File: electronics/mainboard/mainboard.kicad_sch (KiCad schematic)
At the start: 1 part, among them U1 1022

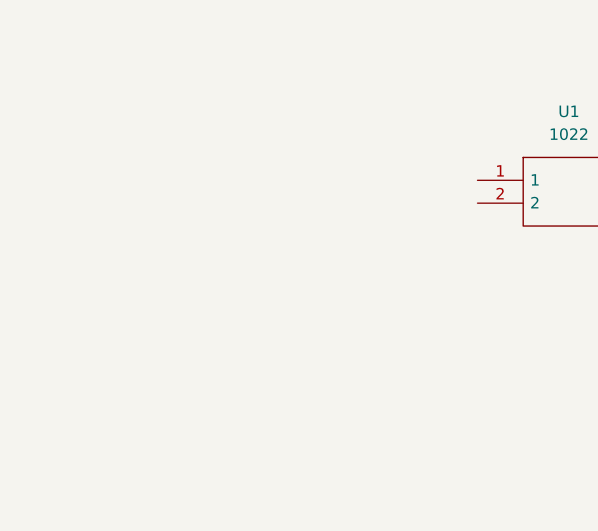
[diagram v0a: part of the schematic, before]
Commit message: add arduino nano to pcb
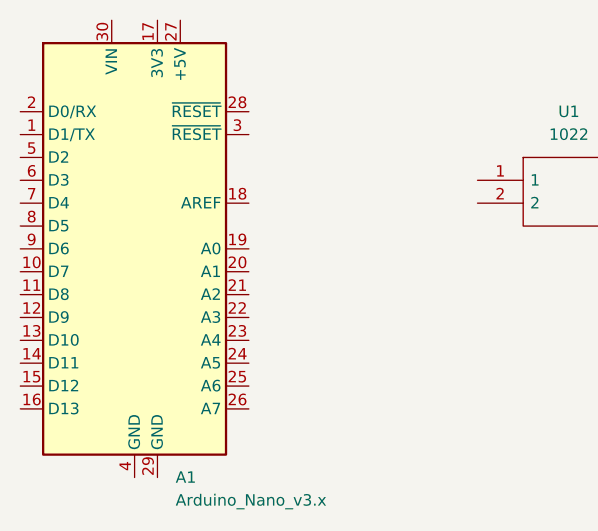
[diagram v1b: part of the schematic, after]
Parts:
- added A1: Arduino_Nano_v3.x, Module:Arduino_Nano_WithMountingHoles, symbol MCU_Module:Arduino_Nano_v3.x
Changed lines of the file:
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@@
     (pin "4")
+  )
+  (symbol (lib_id "MCU_Module:Arduino_Nano_v3.x") (at 106.68 95.25 0) (unit 1)
+    (in_bom yes) (on_board yes) (fields_autoplaced)
+    (property "Reference" "A1" (id 0) (at 111.2394 120.65 0)
+      (effects (font (size 1.27 1.27)) (justify left))
+    )
+    (property "Value" "Arduino_Nano_v3.x" (id 1) (at 111.2394 123.19 0)
+      (effects (font (size 1.27 1.27)) (justify left))
+    )
+    (property "Footprint" "Module:Arduino_Nano_WithMountingHoles" (id 2) (at 106.68 95.25 0)
+      (effects (font (size 1.27 1.27) italic) hide)
+    )
+    (property "Datasheet" "http://www.mouser.com/pdfdocs/Gravitech_Arduino_Nano3_0.pdf" (id 3) (at 106.68 95.25 0)
+      (effects (font (size 1.27 1.27)) hide)
+    )
+    (pin "1")
+    (pin "10")
+    (pin "11")
+    (pin "12")
+    (pin "13")
+    (pin "14")
+    (pin "15")
+    (pin "16")
+    (pin "17")
+    (pin "18")
+    (pin "19")
+    (pin "2")
+    (pin "20")
+    (pin "21")
+    (pin "22")
+    (pin "23")
+    (pin "24")
+    (pin "25")
+    (pin "26")
+    (pin "27")
+    (pin "28")
+    (pin "29")
+    (pin "3")
+    (pin "30")
+    (pin "4")
+    (pin "5")
+    (pin "6")
+    (pin "7")
+    (pin "8")
+    (pin "9")
   )
   (sheet_instances
@@
   )
   (symbol_instances
+    (path "/8fac398c-22c9-4741-a001-aab7ea92da04"
+      (reference "A1") (unit 1) (value "Arduino_Nano_v3.x") (footprint "Module:Arduino_Nano_WithMountingHoles")
+    )
     (path "/59142adb-6887-41fc-851e-9a7f51511d60"
       (reference "U1") (unit 1) (value "1022") (footprint "SamacSys:1022")

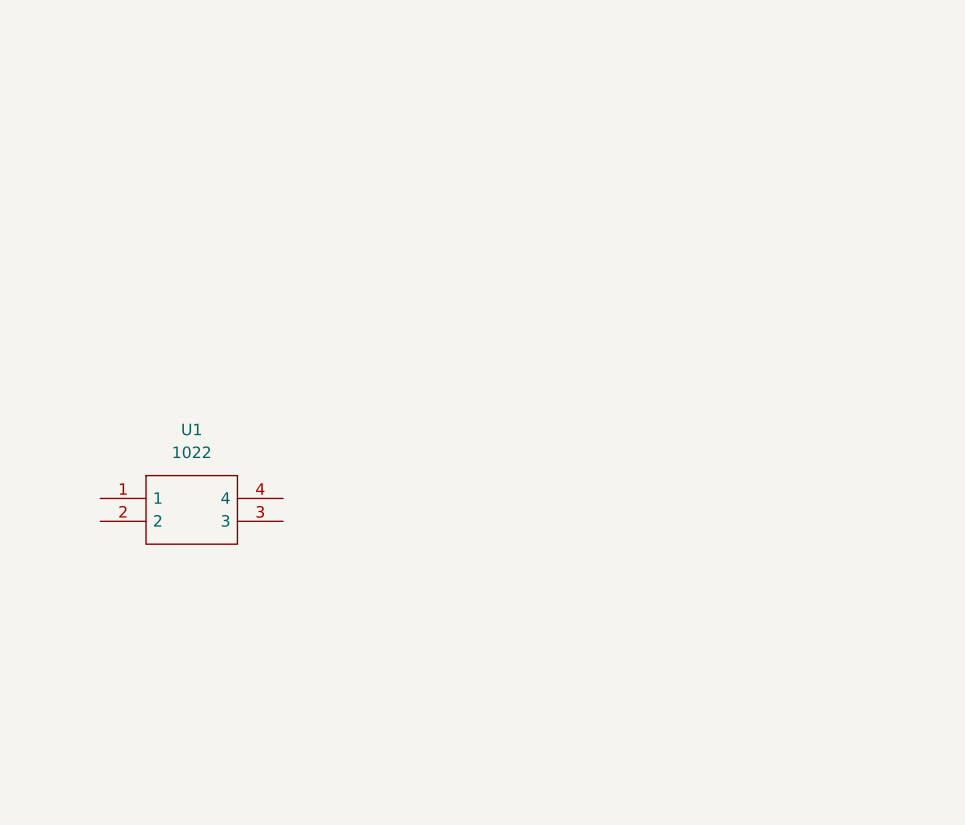
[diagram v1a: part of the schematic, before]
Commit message: add buttons and ir-led
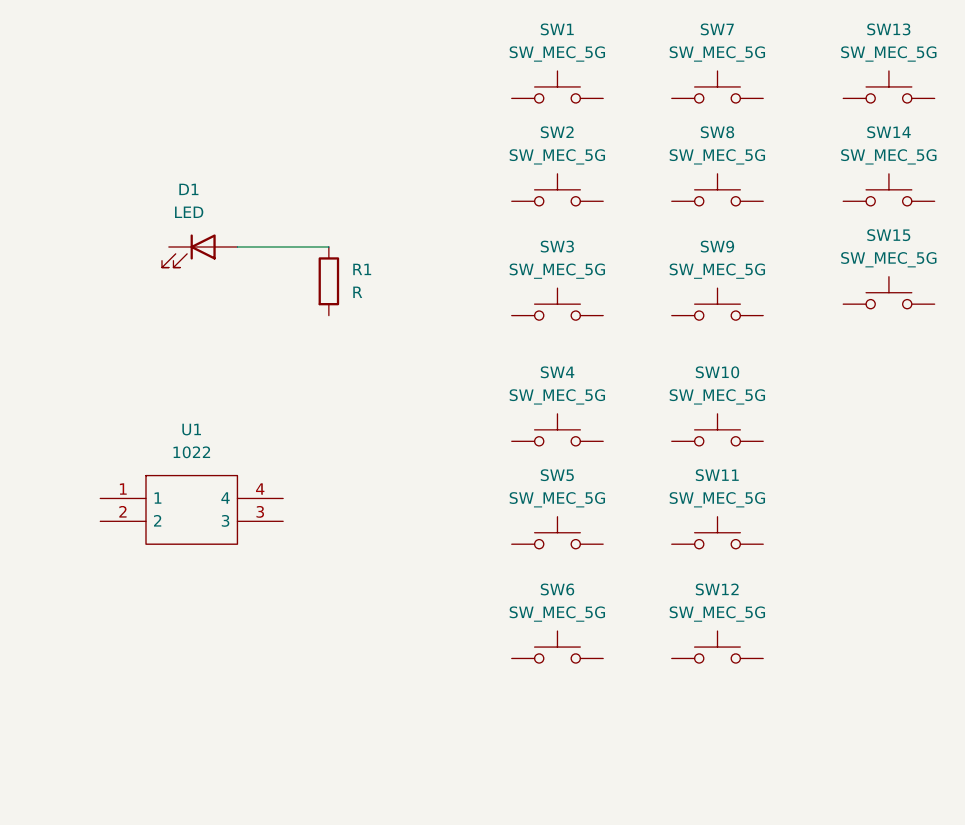
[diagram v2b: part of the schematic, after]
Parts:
- added D1: LED, LED_THT:LED_D5.0mm_Horizontal_O1.27mm_Z3.0mm, symbol Device:LED
- added R1: R, Resistor_SMD:R_0805_2012Metric, symbol Device:R
- added SW1, SW10, SW11, SW12, SW13, SW14, SW15, SW2, SW3, SW4, SW5, SW6, SW7, SW8, SW9: SW_MEC_5G, Button_Switch_THT:SW_PUSH_6mm, symbol Switch:SW_MEC_5G
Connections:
- new net: SW11.1 (A), SW11.2 (A)
- new net: SW11.3 (B), SW11.4 (B)
- new net: D1.2 (A), R1.1
- new net: SW5.1 (A), SW5.2 (A)
- new net: SW5.3 (B), SW5.4 (B)
- new net: SW2.1 (A), SW2.2 (A)
- new net: SW2.3 (B), SW2.4 (B)
- new net: SW8.1 (A), SW8.2 (A)
- new net: SW8.3 (B), SW8.4 (B)
- new net: SW3.1 (A), SW3.2 (A)
- new net: SW3.3 (B), SW3.4 (B)
- new net: SW7.1 (A), SW7.2 (A)
- new net: SW7.3 (B), SW7.4 (B)
- new net: SW12.1 (A), SW12.2 (A)
- new net: SW12.3 (B), SW12.4 (B)
- new net: SW9.1 (A), SW9.2 (A)
- new net: SW9.3 (B), SW9.4 (B)
- new net: SW10.1 (A), SW10.2 (A)
- new net: SW10.3 (B), SW10.4 (B)
- new net: SW13.1 (A), SW13.2 (A)
- new net: SW13.3 (B), SW13.4 (B)
- new net: SW14.1 (A), SW14.2 (A)
- new net: SW14.3 (B), SW14.4 (B)
- new net: SW15.1 (A), SW15.2 (A)
- new net: SW15.3 (B), SW15.4 (B)
- new net: SW4.1 (A), SW4.2 (A)
- new net: SW4.3 (B), SW4.4 (B)
- new net: SW1.1 (A), SW1.2 (A)
- new net: SW1.3 (B), SW1.4 (B)
- new net: SW6.1 (A), SW6.2 (A)
- new net: SW6.3 (B), SW6.4 (B)

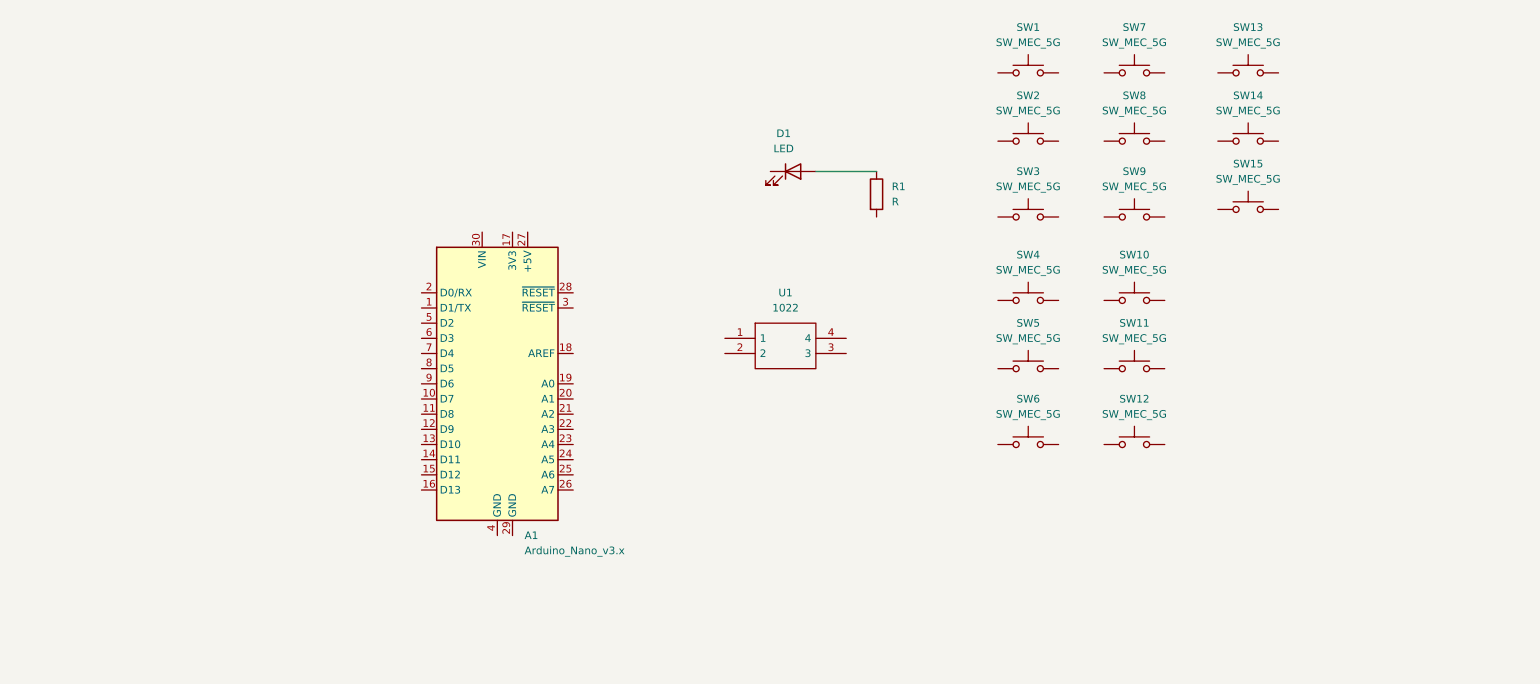
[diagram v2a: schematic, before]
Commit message: add schematic connections
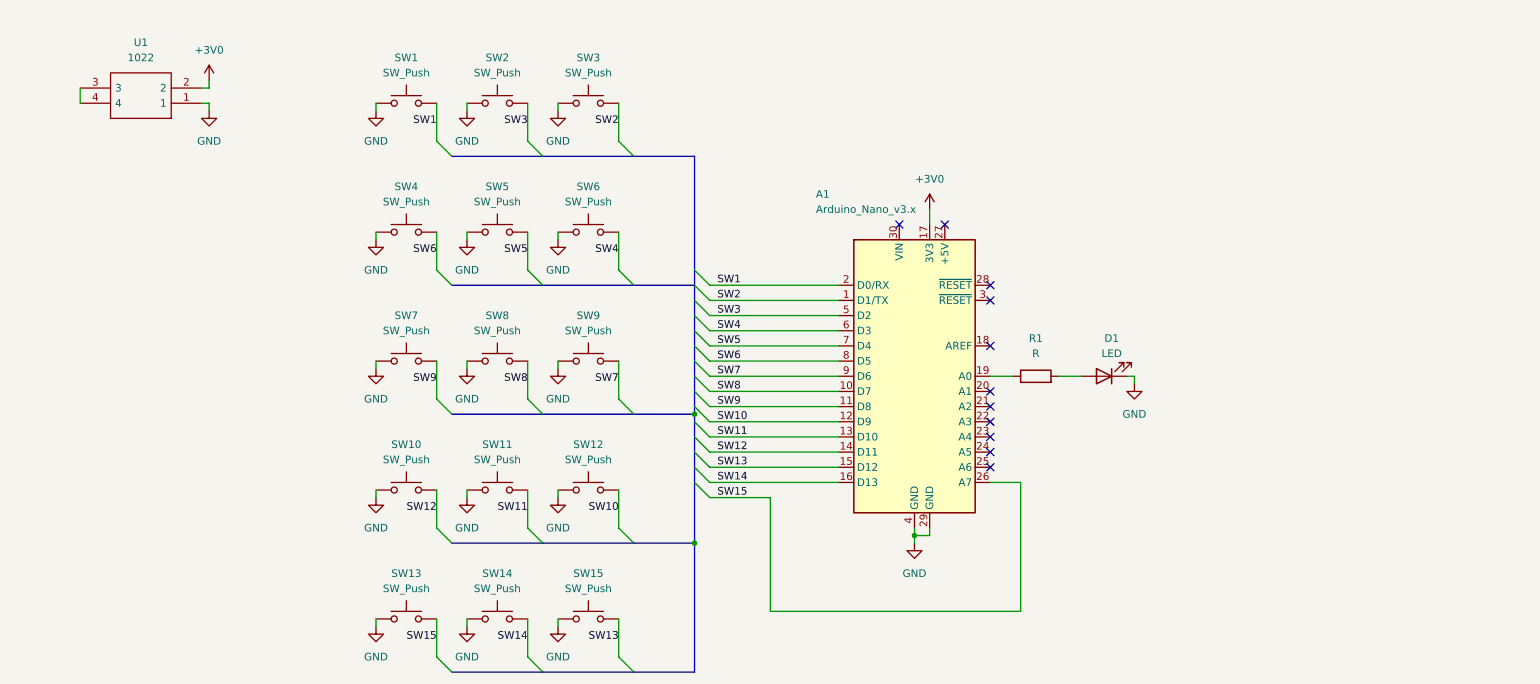
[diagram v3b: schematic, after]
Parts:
- removed SW1, SW10, SW11, SW12, SW13, SW14, SW15, SW2, SW3, SW4, SW5, SW6, SW7, SW8, SW9: SW_MEC_5G, Button_Switch_THT:SW_PUSH_6mm, symbol Switch:SW_MEC_5G
- added SW1, SW10, SW11, SW12, SW13, SW14, SW15, SW2, SW3, SW4, SW5, SW6, SW7, SW8, SW9: SW_Push, Button_Switch_THT:SW_PUSH_6mm, symbol Switch:SW_Push
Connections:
- net at R1.1: now also A1.19 (A0); no longer D1.2 (A)
- net at R1.2: now also D1.2 (A)
- net GND: now reaches U1.1
- net GND: now also A1.29 (GND), A1.4 (GND), D1.1 (K), SW1.1, SW10.1, SW11.1, SW12.1, SW13.1, SW14.1, SW15.1, SW2.1, SW3.1, SW4.1, SW5.1, SW6.1, SW7.1, SW8.1, SW9.1
- net +3V0: now reaches U1.2
- net +3V0: now also A1.17 (3V3)
- net at U1.3: now also U1.4
- net SW2: now reaches A1.1 (D1/TX)
- net SW2: now also SW3.2
- net SW8: now reaches A1.10 (D7)
- net SW8: now also SW8.2
- net SW9: now reaches A1.11 (D8)
- net SW9: now also SW7.2
- net SW10: now reaches A1.12 (D9)
- net SW10: now also SW12.2
- net SW11: now reaches A1.13 (D10)
- net SW11: now also SW11.2
- net SW12: now reaches A1.14 (D11)
- net SW12: now also SW10.2
- net SW13: now reaches A1.15 (D12)
- net SW13: now also SW15.2
- net SW14: now reaches A1.16 (D13)
- net SW14: now also SW14.2
- net SW1: now reaches A1.2 (D0/RX)
- net SW1: now also SW1.2
- net SW15: now reaches A1.26 (A7)
- net SW15: now also SW13.2
- net SW3: now reaches A1.5 (D2)
- net SW3: now also SW2.2
- net SW4: now reaches A1.6 (D3)
- net SW4: now also SW6.2
- net SW5: now reaches A1.7 (D4)
- net SW5: now also SW5.2
- net SW6: now reaches A1.8 (D5)
- net SW6: now also SW4.2
- net SW7: now reaches A1.9 (D6)
- net SW7: now also SW9.2
- no-connect marks 0 -> 11
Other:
- moved on the sheet: A1, D1, R1, U1

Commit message: add polarity protection
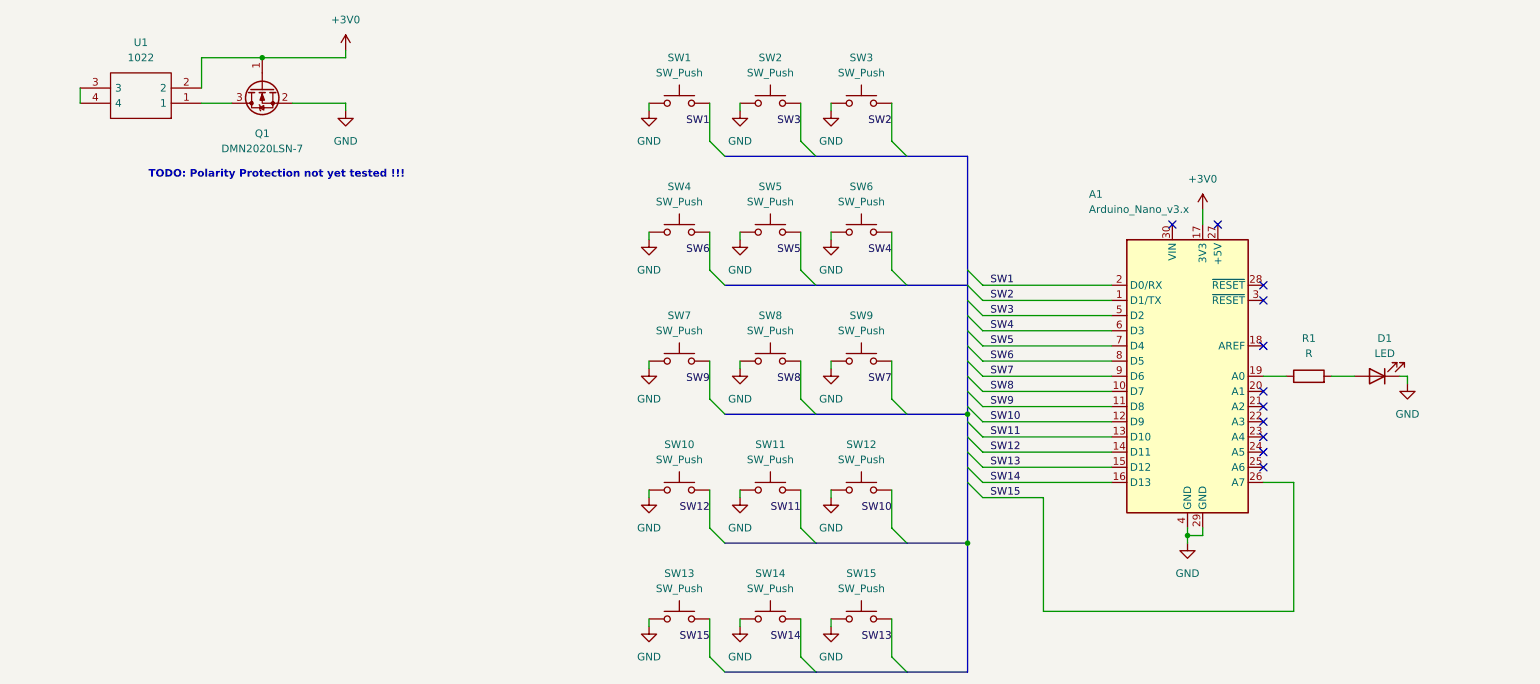
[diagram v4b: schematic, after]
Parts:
- added Q1: DMN2020LSN-7, Package_TO_SOT_SMD:SOT-23, symbol Transistor_FET:DMN2041L
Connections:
- net +3V0: now also Q1.1 (G)
- net GND: now also Q1.2 (S); no longer U1.1
- new net: Q1.3 (D), U1.1
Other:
- note added: "TODO: Polarity Protection not yet tested !!!"
- moved on the sheet: A1, D1, R1, SW1, SW10, SW11, SW12, SW13, SW14, SW15, SW2, SW3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

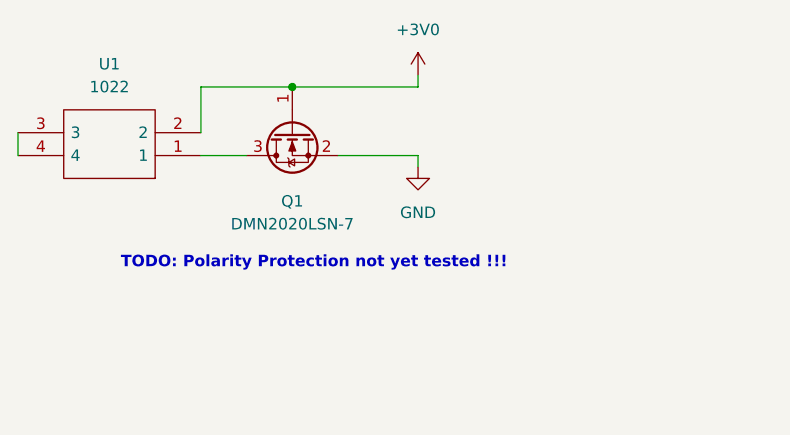
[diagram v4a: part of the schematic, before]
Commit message: clean up libraries and  add more parts to desing - clean up libraries folder structure - no longer ignore important library table files - ignore auto save files - add fet for polarity protection - add buffer capacitors
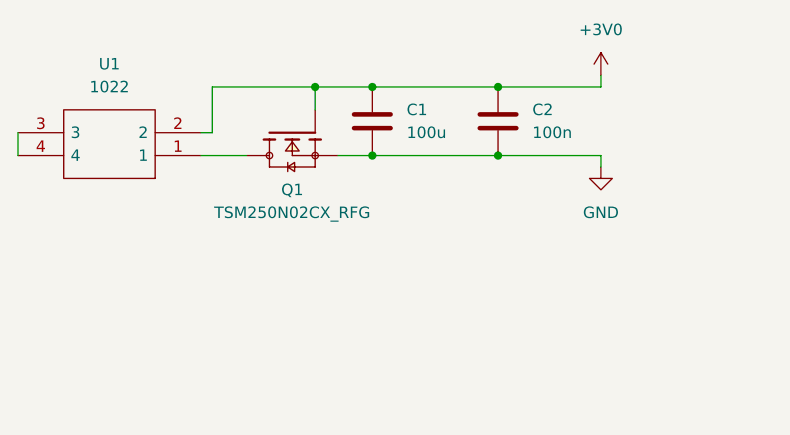
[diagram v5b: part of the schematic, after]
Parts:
- removed Q1: DMN2020LSN-7, Package_TO_SOT_SMD:SOT-23, symbol Transistor_FET:DMN2041L
- added C1: 100u, Capacitor_SMD:C_0805_2012Metric, symbol Device:C
- added C2: 100n, Capacitor_SMD:C_0805_2012Metric, symbol Device:C
- added Q1: TSM250N02CX_RFG, TSM250N02CX_RFG:TRANS_TSM250N02CX_RFG, symbol TSM250N02CX_RFG:TSM250N02CX_RFG
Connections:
- net +3V0: now also C1.1, C2.1, Q1.1
- net GND: now also C1.2, C2.2, Q1.2
- net at U1.1: now also Q1.3
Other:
- note removed: "TODO: Polarity Protection not yet tested !!!"

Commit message: driver for ir-led and minor optimizations
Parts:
- added JP1: SolderJumper_2_Bridged, Jumper:SolderJumper-2_P1.3mm_Bridged_Pad1.0x1.5mm, symbol Jumper:SolderJumper_2_Bridged
- added Q2: TSM250N02CX_RFG, TSM250N02CX_RFG:TRANS_TSM250N02CX_RFG, symbol TSM250N02CX_RFG:TSM250N02CX_RFG
- D1: value LED -> IR333-A
- R1: value R -> 82 1% 35mW
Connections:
- net +3V0: now also R1.2, JP1.2 (B); no longer U1.2
- net GND: now also Q2.2; no longer D1.1 (K)
- net at R1.1: now also D1.2 (A); no longer A1.19 (A0)
- new net: JP1.1 (A), U1.2
- new net: D1.1 (K), Q2.3
- new net: A1.19 (A0), Q2.1
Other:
- moved on the sheet: D1, R1, U1

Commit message: route pcb
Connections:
- net SW1: now also A1.7 (D4); no longer A1.2 (D0/RX)
- net SW10: now also A1.2 (D0/RX), SW10.2; no longer A1.12 (D9), SW12.2
- net SW11: now also A1.9 (D6); no longer A1.13 (D10)
- net SW12: now also SW12.2; no longer SW10.2
- net SW13: now also A1.1 (D1/TX), SW13.2; no longer A1.15 (D12), SW15.2
- net SW14: now also A1.8 (D5); no longer A1.16 (D13)
- net SW15: now also A1.13 (D10), SW15.2; no longer A1.26 (A7), SW13.2
- net SW2: now also A1.12 (D9), SW2.2; no longer A1.1 (D1/TX), SW3.2
- net SW3: now also A1.25 (A6), SW3.2; no longer A1.5 (D2), SW2.2
- net SW4: now also SW4.2; no longer SW6.2
- net SW5: now also A1.11 (D8); no longer A1.7 (D4)
- net SW6: now also A1.24 (A5), SW6.2; no longer A1.8 (D5), SW4.2
- net SW7: now also A1.5 (D2), SW7.2; no longer A1.9 (D6), SW9.2
- net SW9: now also A1.15 (D12), SW9.2; no longer A1.11 (D8), SW7.2
- net at A1.19 (A0): no longer Q2.1
- new net: A1.26 (A7), Q2.1
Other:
- moved on the sheet: D1, Q2, R1
